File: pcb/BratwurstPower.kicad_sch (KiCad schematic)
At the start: 23 parts, among them J1 BarrelJack, J2 Raspi, J3 Power IN, J4 USB1in, J5 USB1out, J6 USB2in, J7 USB2out, J8 EXT

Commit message: fix: replace overlapping footprints with custom one
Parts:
- removed J3: Power IN, TerminalBlock_RND:TerminalBlock_RND_205-00001_1x02_P5.00mm_Horizontal, symbol Connector_Generic:Conn_01x02
- J1: footprint Connector_BarrelJack:BarrelJack_Horizontal -> BratwurstPower:BarrelJack_Combined
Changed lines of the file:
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@@
 	(generator_version "8.0")
 	(paper "A4")
-    (title_block
-                (title "BratwurstPower")
-                (date "${DATE}")
-                (rev "${VERSION}")
-                (company "Qetesh")
-            )
+	(title_block
+		(title "BratwurstPower")
+		(date "${DATE}")
+		(rev "${VERSION}")
+		(company "Qetesh")
+	)
 	(junction
 		(at 121.92 135.89)
@@
 	(wire
 		(pts
-			(xy 71.12 69.85) (xy 107.95 69.85)
-		)
-		(stroke
-			(width 0)
-			(type default)
-		)
-	)
-	(wire
-		(pts
 			(xy 170.18 86.36) (xy 170.18 85.09)
 		)
@@
 	(wire
 		(pts
-			(xy 72.39 72.39) (xy 71.12 72.39)
-		)
-		(stroke
-			(width 0)
-			(type default)
-		)
-	)
-	(wire
-		(pts
 			(xy 146.05 36.83) (xy 193.04 36.83)
 		)
@@
 	(wire
 		(pts
-			(xy 72.39 74.93) (xy 72.39 72.39)
-		)
-		(stroke
-			(width 0)
-			(type default)
-		)
-	)
-	(wire
-		(pts
 			(xy 121.92 87.63) (xy 124.46 87.63)
 		)
@@
 			)
 		)
-		(property "Footprint" "Connector_BarrelJack:BarrelJack_Horizontal"
+		(property "Footprint" "BratwurstPower:BarrelJack_Combined"
 			(at 63.5 40.386 0)
 			(effects
@@
 	)
 	(symbol
-		(lib_id "Connector_Generic:Conn_01x02")
-		(at 66.04 69.85 0)
-		(mirror y)
-		(unit 1)
-		(exclude_from_sim no)
-		(in_bom yes)
-		(on_board yes)
-		(dnp no)
-		(fields_autoplaced yes)
-		(property "Reference" "J3"
-			(at 63.5 69.8499 0)
-			(effects
-				(font
-					(size 1.27 1.27)
-				)
-				(justify left)
-			)
-		)
-		(property "Value" "Power IN"
-			(at 63.5 72.3899 0)
-			(effects
-				(font
-					(size 1.27 1.27)
-				)
-				(justify left)
-			)
-		)
-		(property "Footprint" "TerminalBlock_RND:TerminalBlock_RND_205-00001_1x02_P5.00mm_Horizontal"
-			(at 66.04 69.85 0)
-			(effects
-				(font
-					(size 1.27 1.27)
-				)
-				(hide yes)
-			)
-		)
-		(property "Datasheet" "~"
-			(at 66.04 69.85 0)
-			(effects
-				(font
-					(size 1.27 1.27)
-				)
-				(hide yes)
-			)
-		)
-		(property "Description" "Generic connector, single row, 01x02, script generated (kicad-library-utils/schlib/autogen/connector/)"
-			(at 66.04 69.85 0)
-			(effects
-				(font
-					(size 1.27 1.27)
-				)
-				(hide yes)
-			)
-		)
-		(pin "2"
-		)
-		(pin "1"
-		)
-		(instances
-			(project ""
-				(path "/d3b20f0a-e666-4f64-bba3-6679d961a6dd"
-					(reference "J3")
-					(unit 1)
-				)
-			)
-		)
-	)
-	(symbol
 		(lib_id "power:GND")
 		(at 200.66 120.65 0)
@@
 					(unit 1)
 				)
-			)
-		)
-	)
-	(symbol
-		(lib_id "power:GND")
-		(at 72.39 74.93 0)
-		(unit 1)
-		(exclude_from_sim no)
-		(in_bom yes)
-		(on_board yes)
-		(dnp no)
-		(fields_autoplaced yes)
-		(property "Reference" "#PWR04"
-			(at 72.39 81.28 0)
-			(effects
-				(font
-					(size 1.27 1.27)
-				)
-				(hide yes)
-			)
-		)
-		(property "Value" "GND"
-			(at 72.39 80.01 0)
-			(effects
-				(font
-					(size 1.27 1.27)
-				)
-			)
-		)
-		(property "Footprint" ""
-			(at 72.39 74.93 0)
-			(effects
-				(font
-					(size 1.27 1.27)
-				)
-				(hide yes)
-			)
-		)
-		(property "Datasheet" ""
-			(at 72.39 74.93 0)
-			(effects
-				(font
-					(size 1.27 1.27)
-				)
-				(hide yes)
-			)
-		)
-		(property "Description" "Power symbol creates a global label with name \"GND\" , ground"
-			(at 72.39 74.93 0)
-			(effects
-				(font
-					(size 1.27 1.27)
-				)
-				(hide yes)
-			)
-		)
-		(pin "1"
-		)
-		(instances
-			(project "RaspiPowerSupply"
-				(path "/d3b20f0a-e666-4f64-bba3-6679d961a6dd"
-					(reference "#PWR04")
-					(unit 1)
-				)

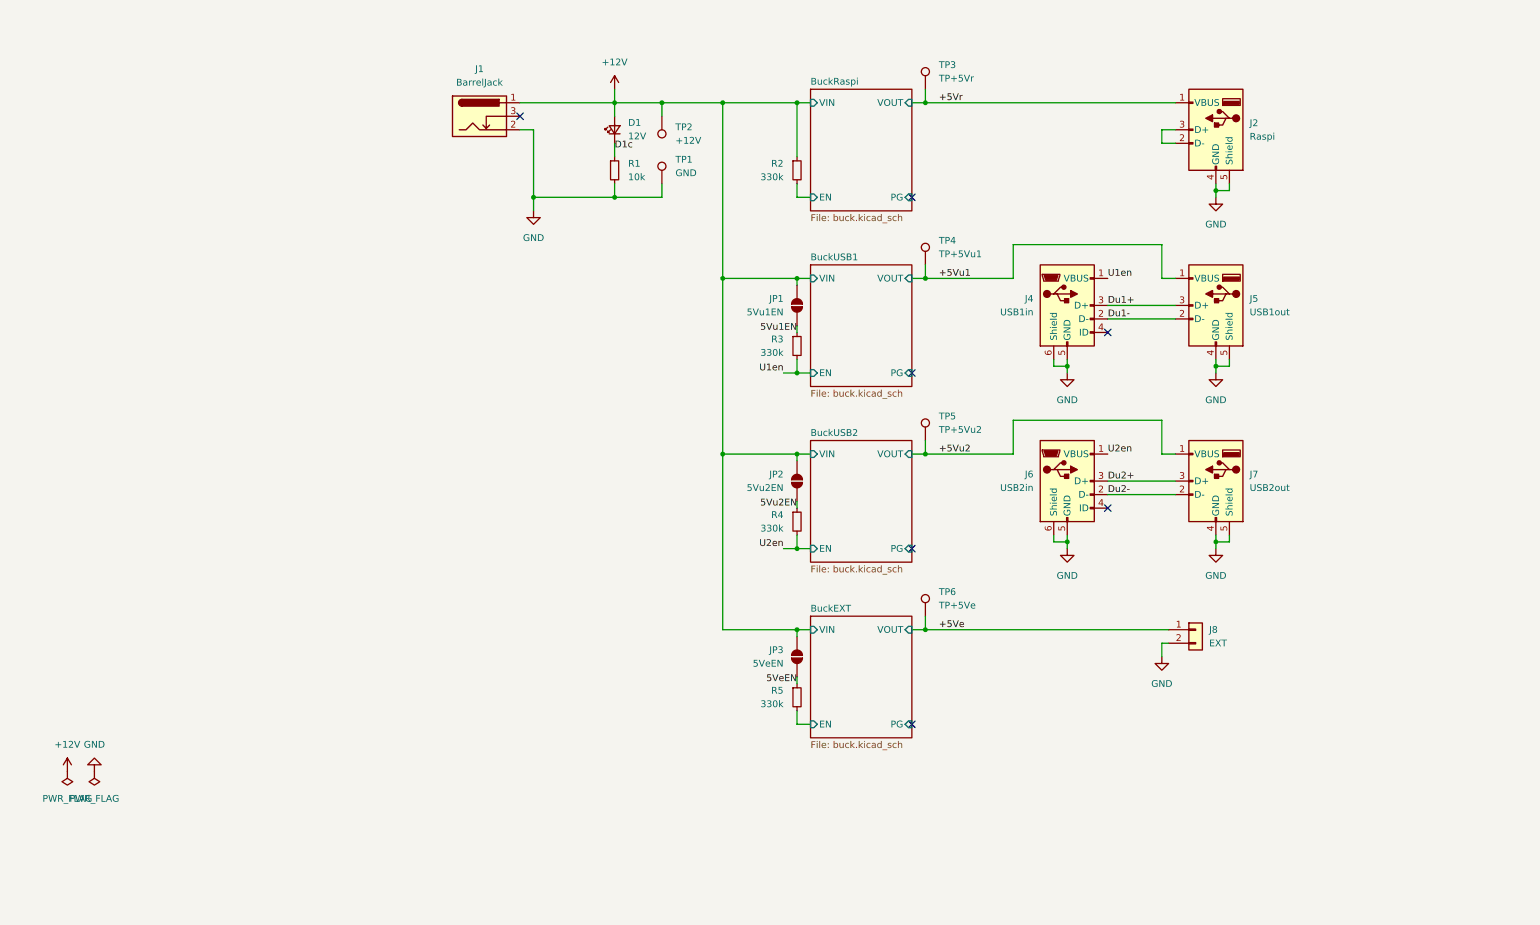
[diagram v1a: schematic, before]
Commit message: feat: add more functionality
- INA power monitor on each output
- I/O expander to reset usb ports if needed
- Bratwurst Logo
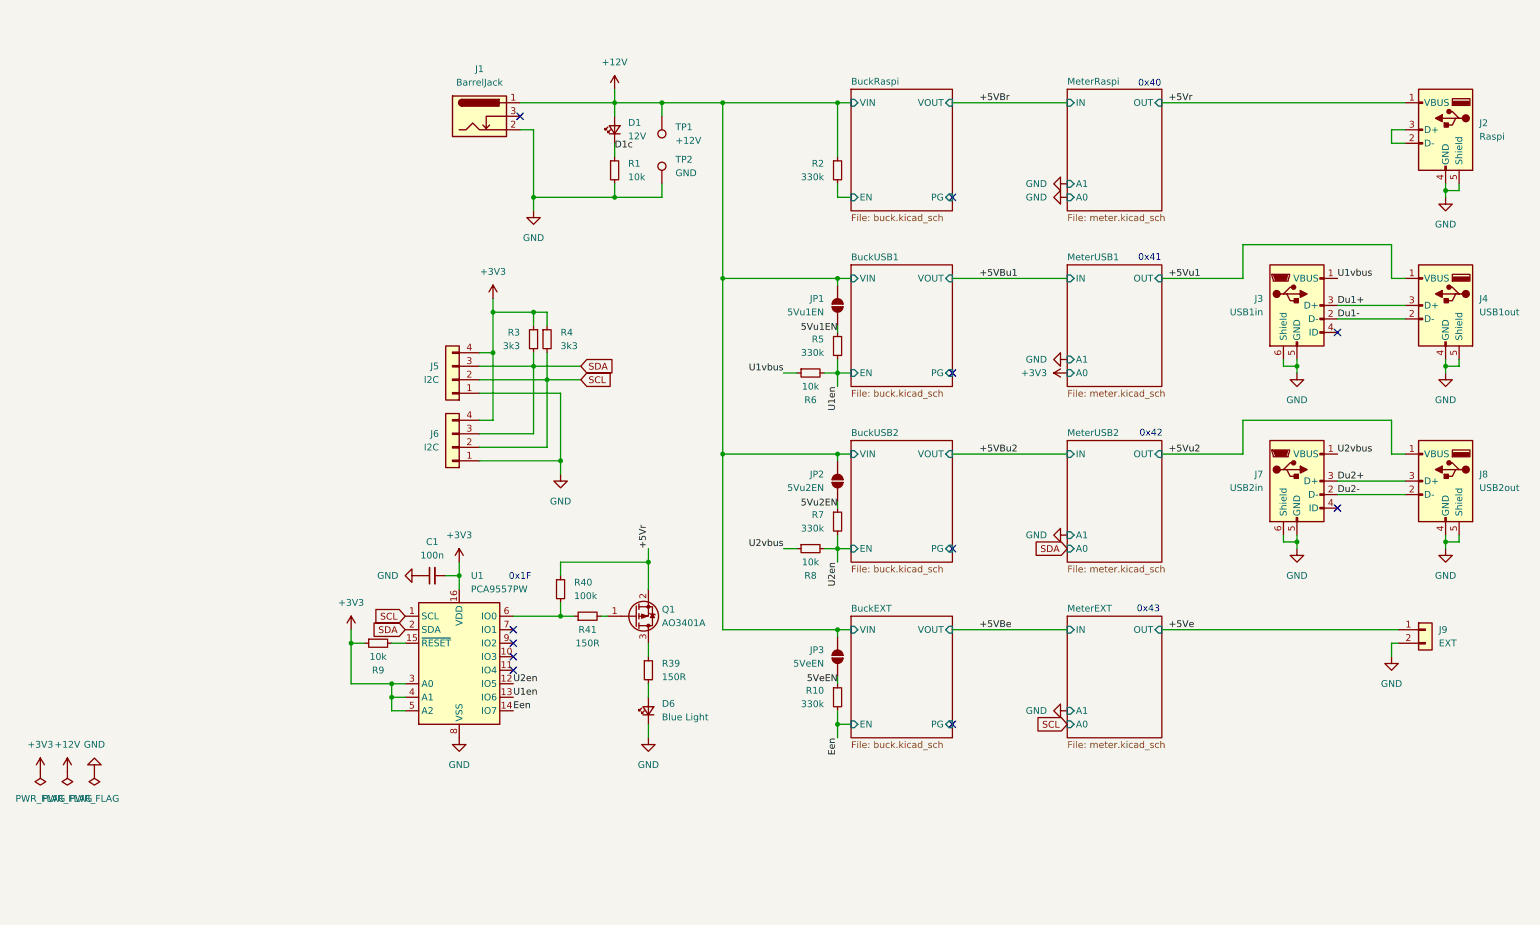
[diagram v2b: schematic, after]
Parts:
- removed TP3: TP+5Vr, TestPoint:TestPoint_Pad_D1.5mm, symbol Connector:TestPoint
- removed TP4: TP+5Vu1, TestPoint:TestPoint_Pad_D1.5mm, symbol Connector:TestPoint
- removed TP5: TP+5Vu2, TestPoint:TestPoint_Pad_D1.5mm, symbol Connector:TestPoint
- removed TP6: TP+5Ve, TestPoint:TestPoint_Pad_D1.5mm, symbol Connector:TestPoint
- added C1: 100n, Capacitor_SMD:C_0402_1005Metric, symbol Device:C_Small
- added D6: Blue Light, LED_SMD:LED_0805_2012Metric, symbol Device:LED_Small
- added J5, J6: I2C, Connector_JST:JST_PH_S4B-PH-K_1x04_P2.00mm_Horizontal, symbol Connector_Generic:Conn_01x04
- added Q1: AO3401A, Package_TO_SOT_SMD:SOT-23, symbol Transistor_FET:AO3401A
- added R3, R4: 3k3, Resistor_SMD:R_0402_1005Metric, symbol Device:R_Small
- added R39, R41: 150R, Resistor_SMD:R_0402_1005Metric, symbol Device:R_Small
- added R40: 100k, Resistor_SMD:R_0402_1005Metric, symbol Device:R_Small
- added R6, R8, R9: 10k, Resistor_SMD:R_0402_1005Metric, symbol Device:R_Small
- added U1: PCA9557PW, Package_SO:TSSOP-16_4.4x5mm_P0.65mm, symbol Interface_Expansion:PCA9557PW
- renumbered J4 to J3, J5 to J4, J6 to J7, J7 to J8, J8 to J9, R5 to R10, R3 to R5, R4 to R7, TP2 to TP1, TP1 to TP2
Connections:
- net +5Vr: now also Q1.2 (S), R40.1
- net GND: now also C1.1, D6.1 (K), J5.1 (Pin_1), J6.1 (Pin_1), U1.8 (VSS)
- net U1en: now also R6.2, U1.13 (IO6); no longer J3.1 (VBUS)
- net U2en: now also R8.2, U1.12 (IO5); no longer J7.1 (VBUS)
- net BuckEXT/EN renamed Een
- net Een: now also U1.14 (IO7)
- new net: Q1.1 (G), R41.2
- new net: Q1.3 (D), R39.1
- new net: R9.2, U1.15 (~{RESET})
- new net: R40.2, R41.1, U1.6 (IO0)
- new net: D6.2 (A), R39.2
- new net +3V3: C1.2, J5.4 (Pin_4), J6.4 (Pin_4), R3.1, R4.1, R9.1, U1.16 (VDD), U1.3 (A0), U1.4 (A1), U1.5 (A2)
- new net SCL: J5.2 (Pin_2), J6.2 (Pin_2), R4.2, U1.1 (SCL)
- new net SDA: J5.3 (Pin_3), J6.3 (Pin_3), R3.2, U1.2 (SDA)
- new net U1vbus: J3.1 (VBUS), R6.1
- new net U2vbus: J7.1 (VBUS), R8.1
- no-connect marks 7 -> 11
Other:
- added sheet MeterEXT (meter.kicad_sch)
- added sheet MeterRaspi (meter.kicad_sch)
- added sheet MeterUSB1 (meter.kicad_sch)
- added sheet MeterUSB2 (meter.kicad_sch)
- note added: "0x1F"
- note added: "0x40"
- note added: "0x41"
- note added: "0x42"
- note added: "0x43"
- moved on the sheet: J2, J3, J4, J7, J8, J9, JP1, JP2, JP3, R10, R2, R5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

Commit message: feat: featuritis
added too much stuff...
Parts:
- removed D1: 12V, LED_SMD:LED_0603_1608Metric, symbol Device:LED_Small
- removed R40: 100k, Resistor_SMD:R_0402_1005Metric, symbol Device:R_Small
- removed R41: 150R, Resistor_SMD:R_0402_1005Metric, symbol Device:R_Small
- added D1: MM3Z10, Diode_SMD:D_SOD-323F, symbol Diode:MM3Zxx
- added J10: GPIO, Connector_PinHeader_2.54mm:PinHeader_1x06_P2.54mm_Vertical, symbol Connector_Generic:Conn_01x06
- added TP3: +5Vu2, TestPoint:TestPoint_THTPad_D1.0mm_Drill0.5mm, symbol Connector:TestPoint
- added TP4: +5Ve, TestPoint:TestPoint_THTPad_D1.0mm_Drill0.5mm, symbol Connector:TestPoint
- added TP5: +12V, TestPoint:TestPoint_THTPad_D2.0mm_Drill1.0mm, symbol Connector:TestPoint
- added TP6: GND, TestPoint:TestPoint_THTPad_D2.0mm_Drill1.0mm, symbol Connector:TestPoint
- R1: value 10k -> 100k; LCSC C25744 -> (none)
- TP1: value +12V -> +5Vr; footprint TestPoint:TestPoint_Pad_D1.5mm -> TestPoint:TestPoint_THTPad_D1.0mm_Drill0.5mm; now in the parts list
- TP2: value GND -> +5Vu1; footprint TestPoint:TestPoint_Pad_D1.5mm -> TestPoint:TestPoint_THTPad_D1.0mm_Drill0.5mm; now in the parts list
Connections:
- net D1c is gone; now on net Q1g: R1.1
- net +12V: no longer J1.1, TP1.1
- net +3V3: now also J10.1 (Pin_1)
- net +5Ve: now also TP4.1
- net +5Vr: now also D6.2 (A), TP1.1; no longer Q1.2 (S)
- net +5Vu1: now also TP2.1
- net +5Vu2: now also TP3.1
- net GND: now also J10.6 (Pin_6), TP6.1; no longer D6.1 (K), TP2.1
- net Q1g: now reaches Q1.1 (G)
- net Q1g: now also D1.2 (A)
- net at R39.1: now also D6.1 (K); no longer Q1.3 (D)
- net IO3: now reaches U1.10 (IO3)
- net IO3: now also J10.4 (Pin_4)
- net IO4: now reaches U1.11 (IO4)
- net IO4: now also J10.5 (Pin_5)
- net ~{BLen}: now reaches U1.6 (IO0)
- net ~{BLen}: now also R39.2
- net IO1: now reaches U1.7 (IO1)
- net IO1: now also J10.2 (Pin_2)
- net IO2: now reaches U1.9 (IO2)
- net IO2: now also J10.3 (Pin_3)
- new net +12Vin: J1.1, Q1.3 (D), TP5.1
- new net +12Vpp: D1.1 (K), Q1.2 (S)
- no-connect marks 11 -> 7
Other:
- added sheet MeterMain (meter.kicad_sch)
- note added: "0x44"
- moved on the sheet: C1, D6, J1, J2, J3, J4, J5, J6, J7, J8, J9, JP1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

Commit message: chore: cleanup
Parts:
- D1: LCSC (none) -> C19077459
- Q1: LCSC (none) -> C15127
- R1: LCSC (none) -> C25741
- R39: LCSC (none) -> C25082
- TP1, TP2, TP3, TP4, TP5, TP6: now left out of the parts list
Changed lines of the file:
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@@
 			)
 		)
+		(property "LCSC" "C19077459"
+			(at 50.8 34.29 0)
+			(effects
+				(font
+					(size 1.27 1.27)
+				)
+				(hide yes)
+			)
+		)
 		(pin "1"
 		)
@@
 		(unit 1)
 		(exclude_from_sim no)
-		(in_bom yes)
+		(in_bom no)
 		(on_board yes)
 		(dnp no)
@@
 		(unit 1)
 		(exclude_from_sim no)
-		(in_bom yes)
+		(in_bom no)
 		(on_board yes)
 		(dnp no)
@@
 		(unit 1)
 		(exclude_from_sim no)
-		(in_bom yes)
+		(in_bom no)
 		(on_board yes)
 		(dnp no)
@@
 		(unit 1)
 		(exclude_from_sim no)
-		(in_bom yes)
+		(in_bom no)
 		(on_board yes)
 		(dnp no)
@@
 			)
 		)
+		(property "LCSC" "C25082"
+			(at 64.77 154.94 0)
+			(effects
+				(font
+					(size 1.27 1.27)
+				)
+				(hide yes)
+			)
+		)
 		(pin "2"
 		)
@@
 		(unit 1)
 		(exclude_from_sim no)
-		(in_bom yes)
+		(in_bom no)
 		(on_board yes)
 		(dnp no)
@@
 			)
 		)
+		(property "LCSC" "C25741"
+			(at 43.18 44.45 0)
+			(effects
+				(font
+					(size 1.27 1.27)
+				)
+				(hide yes)
+			)
+		)
 		(pin "1"
 		)
@@
 			)
 		)
+		(property "LCSC" "C15127"
+			(at 43.18 31.75 0)
+			(effects
+				(font
+					(size 1.27 1.27)
+				)
+				(hide yes)
+			)
+		)
 		(pin "2"
 		)
@@
 		(unit 1)
 		(exclude_from_sim no)
-		(in_bom yes)
+		(in_bom no)
 		(on_board yes)
 		(dnp no)

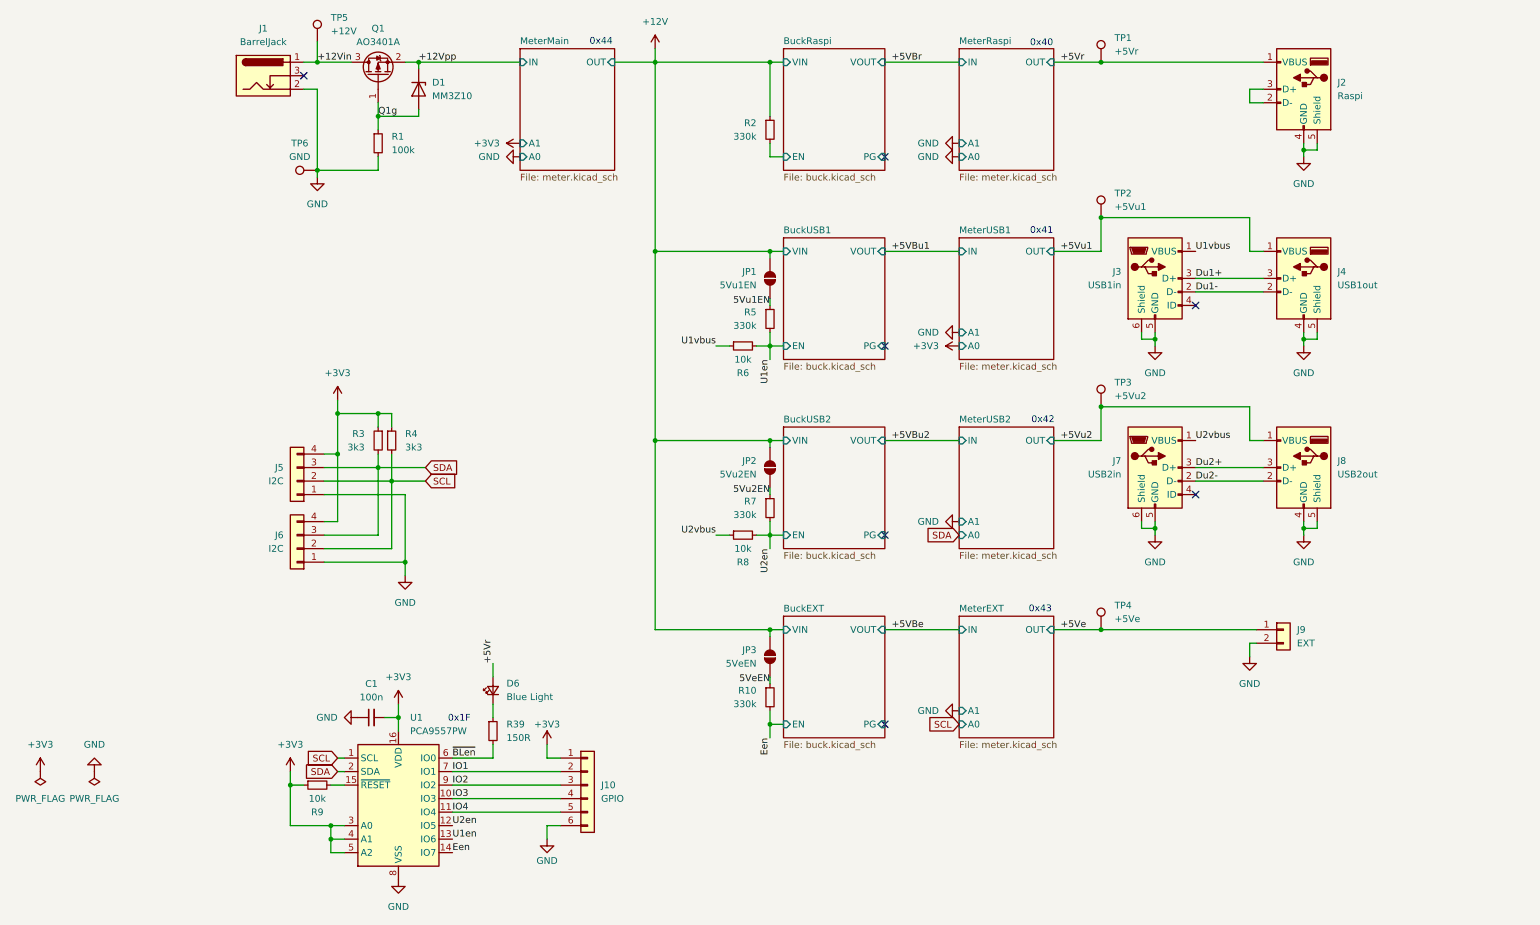
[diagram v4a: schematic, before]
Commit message: feat: add optional input cap
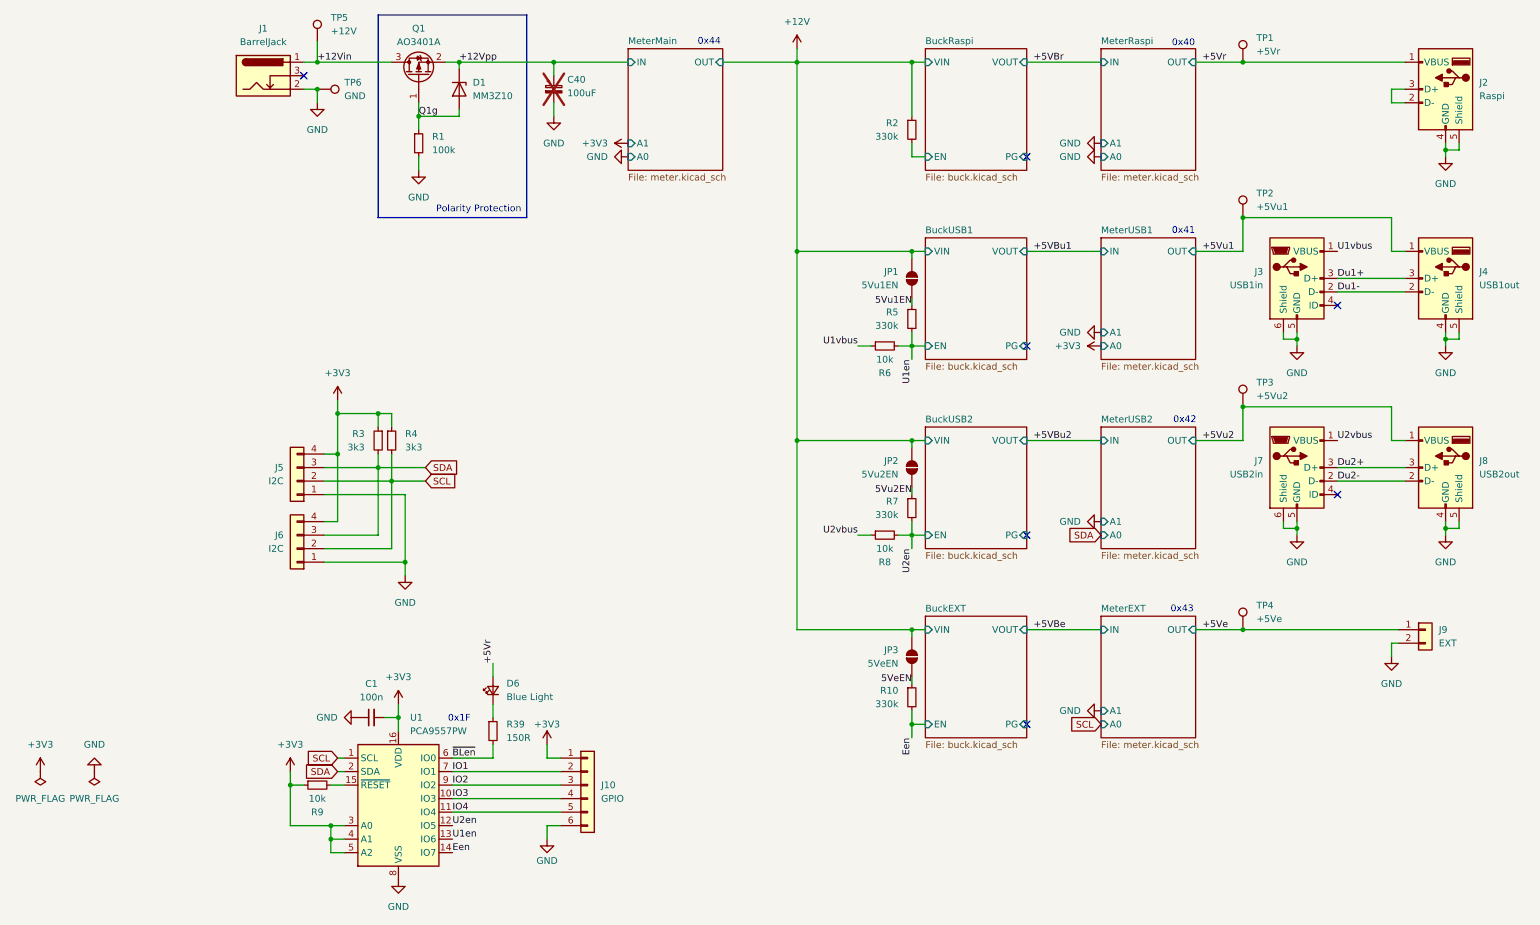
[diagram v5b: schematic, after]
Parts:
- added C40: 100uF, Capacitor_THT:CP_Radial_D6.3mm_P2.50mm, symbol Device:C_Polarized_Small
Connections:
- net +12Vpp: now also C40.1
- net GND: now also C40.2
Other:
- moved on the sheet: D1, J2, J3, J4, J7, J8, J9, JP1, JP2, JP3, Q1, R1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
